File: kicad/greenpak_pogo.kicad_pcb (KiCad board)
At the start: 2 copper layers, 7.6 x 14.5 mm, 6 parts, among them J1 JST_SH_SM04B-SRSS-TB_1x04-1MP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, J2 GREENPAK_POGO_PINS

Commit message: Generated gervers.
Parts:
- turned R1 to -90 degrees
- turned R2 to -90 degrees
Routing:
- net VCC: track 7.47 -> 15.1 mm
- net /SDA: track 13.0 -> 13.6 mm
- net /SCL: track 7.75 -> 8.31 mm
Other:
- board text added: "V0.2"
- board text removed: "V0.1"
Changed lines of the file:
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@@
     (fp_line (start 3 -1.675) (end 3 2.575)
       (stroke (width 0.1) (type solid)) (layer "F.Fab"))
-    (pad "" thru_hole roundrect locked (at -2.8 1.875) (size 1.2 1.8) (drill 0.3) (layers "*.Cu" "F.Paste" "F.Mask") (roundrect_rratio 0.208333))
-    (pad "" thru_hole roundrect locked (at 2.8 1.875) (size 1.2 1.8) (drill 0.3) (layers "*.Cu" "F.Paste" "F.Mask") (roundrect_rratio 0.208333))
+    (pad "" thru_hole roundrect locked (at -2.8 1.875) (size 1.2 1.8) (drill 0.3) (layers "*.Cu" "F.Paste" "F.Mask") (roundrect_rratio 0.2083333333))
+    (pad "" thru_hole roundrect locked (at 2.8 1.875) (size 1.2 1.8) (drill 0.3) (layers "*.Cu" "F.Paste" "F.Mask") (roundrect_rratio 0.2083333333))
     (pad "1" thru_hole roundrect locked (at -1.5 -2) (size 0.6 1.55) (drill 0.3) (layers "*.Cu" "F.Paste" "F.Mask") (roundrect_rratio 0.25)
       (net 1 "GNDD") (pinfunction "Pin_1") (pintype "passive"))
@@
   )
   (footprint "greenpak_pogo:R_0402_1005Metric" (layer "F.Cu")
-    (at 2.54 3.556 90)
+    (at 2.54 3.556 -90)
     (descr "Resistor SMD 0402 (1005 Metric), square (rectangular) end terminal, IPC_7351 nominal, (Body size source: IPC-SM-782 page 72, https://www.pcb-3d.com/wordpress/wp-content/uploads/ipc-sm-782a_amendment_1_and_2.pdf), generated with kicad-footprint-generator")
     (tags "resistor")
@@
     (fp_line (start 0.525 0.27) (end -0.525 0.27)
       (stroke (width 0.1) (type solid)) (layer "F.Fab"))
-    (pad "1" smd roundrect (at -0.51 0 90) (size 0.54 0.64) (layers "F.Cu" "F.Paste" "F.Mask") (roundrect_rratio 0.25)
+    (pad "1" smd roundrect (at -0.51 0 270) (size 0.54 0.64) (layers "F.Cu" "F.Paste" "F.Mask") (roundrect_rratio 0.25)
       (net 5 "VCC") (pintype "passive"))
-    (pad "2" smd roundrect (at 0.51 0 90) (size 0.54 0.64) (layers "F.Cu" "F.Paste" "F.Mask") (roundrect_rratio 0.25)
+    (pad "2" smd roundrect (at 0.51 0 270) (size 0.54 0.64) (layers "F.Cu" "F.Paste" "F.Mask") (roundrect_rratio 0.25)
       (net 4 "/SCL") (pintype "passive"))
     (model "${KICAD6_3DMODEL_DIR}/Resistor_SMD.3dshapes/R_0402_1005Metric.wrl"
@@
   )
   (footprint "greenpak_pogo:R_0402_1005Metric" (layer "F.Cu")
-    (at -2.54 3.556 90)
+    (at -2.54 3.556 -90)
     (descr "Resistor SMD 0402 (1005 Metric), square (rectangular) end terminal, IPC_7351 nominal, (Body size source: IPC-SM-782 page 72, https://www.pcb-3d.com/wordpress/wp-content/uploads/ipc-sm-782a_amendment_1_and_2.pdf), generated with kicad-footprint-generator")
     (tags "resistor")
@@
     (fp_line (start 0.525 0.27) (end -0.525 0.27)
       (stroke (width 0.1) (type solid)) (layer "F.Fab"))
-    (pad "1" smd roundrect (at -0.51 0 90) (size 0.54 0.64) (layers "F.Cu" "F.Paste" "F.Mask") (roundrect_rratio 0.25)
+    (pad "1" smd roundrect (at -0.51 0 270) (size 0.54 0.64) (layers "F.Cu" "F.Paste" "F.Mask") (roundrect_rratio 0.25)
       (net 5 "VCC") (pintype "passive"))
-    (pad "2" smd roundrect (at 0.51 0 90) (size 0.54 0.64) (layers "F.Cu" "F.Paste" "F.Mask") (roundrect_rratio 0.25)
+    (pad "2" smd roundrect (at 0.51 0 270) (size 0.54 0.64) (layers "F.Cu" "F.Paste" "F.Mask") (roundrect_rratio 0.25)
       (net 3 "/SDA") (pintype "passive"))
     (model "${KICAD6_3DMODEL_DIR}/Resistor_SMD.3dshapes/R_0402_1005Metric.wrl"
@@
     (effects (font (size 0.75 0.75) (thickness 0.15)) (justify right mirror))
   )
-  (gr_text "V0.1" (at 0 6.858) (layer "B.SilkS")
+  (gr_text "V0.2" (at 0 6.858) (layer "B.SilkS")
     (effects (font (size 0.75 0.75) (thickness 0.15)) (justify top mirror))
   )
@@
     (effects (font (size 0.75 0.75) (thickness 0.15)) (justify right mirror))
   )
-  (gr_text locked "POGO PINS\nTHIS SIDE" (at 0 1.4732) (layer "B.SilkS")
+  (gr_text locked "POGO PINS\nTHIS SIDE" (at 0 1.397) (layer "B.SilkS")
     (effects (font (size 0.75 0.75) (thickness 0.15)) (justify top mirror))
   )
@@
     (effects (font (size 0.7 0.7) (thickness 0.1)) (justify left bottom))
   )
-  (segment (start -1.7272 1.7272) (end 0 0) (width 0.4064) (layer "F.Cu") (net 1))
-  (segment (start -1.7272 4.6228) (end -1.7272 1.7272) (width 0.4064) (layer "F.Cu") (net 1))
-  (segment (start -1.5 4.85) (end -1.7272 4.6228) (width 0.4064) (layer "F.Cu") (net 1))
-  (segment (start -1.5 5.62) (end -1.5 4.85) (width 0.4064) (layer "F.Cu") (net 1))
+  (segment (start -1.7272 2.6924) (end 0 0.9652) (width 0.4064) (layer "F.Cu") (net 1))
+  (segment (start -1.5 5.62) (end -1.5 4.7632) (width 0.4064) (layer "F.Cu") (net 1))
+  (segment (start -1.7272 4.536) (end -1.7272 2.6924) (width 0.4064) (layer "F.Cu") (net 1))
+  (segment (start 0 0.9652) (end 0 0) (width 0.4064) (layer "F.Cu") (net 1))
+  (segment (start -1.5 4.7632) (end -1.7272 4.536) (width 0.4064) (layer "F.Cu") (net 1))
   (segment (start -0.65 3.175) (end -0.5 3.325) (width 0.4064) (layer "F.Cu") (net 2))
   (segment (start -0.5 3.325) (end -0.5 5.62) (width 0.4064) (layer "F.Cu") (net 2))
-  (segment (start -3.302 6.6548) (end -2.3114 7.6454) (width 0.2032) (layer "F.Cu") (net 3))
-  (segment (start -2.54 3.046) (end -3.0206 3.046) (width 0.2032) (layer "F.Cu") (net 3))
-  (segment (start -3.0206 3.046) (end -3.302 3.3274) (width 0.2032) (layer "F.Cu") (net 3))
-  (segment (start -0.254 7.6454) (end 0.508 6.8834) (width 0.2032) (layer "F.Cu") (net 3))
-  (segment (start -2.54 1.397) (end -2.54 3.046) (width 0.2032) (layer "F.Cu") (net 3))
-  (segment (start -2.3114 7.6454) (end -0.254 7.6454) (width 0.2032) (layer "F.Cu") (net 3))
+  (segment (start -2.286 1.143) (end -3.302 2.159) (width 0.2032) (layer "F.Cu") (net 3))
+  (segment (start -2.6924 4.2184) (end -2.54 4.066) (width 0.254) (layer "F.Cu") (net 3))
   (segment (start 0.508 5.8312) (end 0.508 6.858) (width 0.2032) (layer "F.Cu") (net 3))
-  (segment (start -3.302 3.3274) (end -3.302 6.6548) (width 0.2032) (layer "F.Cu") (net 3))
-  (segment (start -2.54 3.046) (end -2.5146 3.0206) (width 0.254) (layer "F.Cu") (net 3))
-  (segment (start -2.286 1.143) (end -2.54 1.397) (width 0.2032) (layer "F.Cu") (net 3))
+  (segment (start -2.54 4.066) (end -3.3 4.066) (width 0.2032) (layer "F.Cu") (net 3))
+  (segment (start 0.2032 7.4422) (end 0.508 7.1374) (width 0.2032) (layer "F.Cu") (net 3))
+  (segment (start -3.302 2.159) (end -3.302 6.6548) (width 0.2032) (layer "F.Cu") (net 3))
+  (segment (start 0.508 7.1374) (end 0.508 6.8834) (width 0.2032) (layer "F.Cu") (net 3))
+  (segment (start -2.5146 7.4422) (end 0.2032 7.4422) (width 0.2032) (layer "F.Cu") (net 3))
   (segment (start -2.286 0) (end -2.286 1.143) (width 0.2032) (layer "F.Cu") (net 3))
-  (segment (start 3.046 3.046) (end 2.54 3.046) (width 0.2032) (layer "F.Cu") (net 4))
-  (segment (start 2.2286 5.8232) (end 3.302 4.7498) (width 0.2032) (layer "F.Cu") (net 4))
+  (segment (start -3.302 6.6548) (end -2.5146 7.4422) (width 0.2032) (layer "F.Cu") (net 3))
+  (segment (start 2.381 5.8232) (end 3.302 4.9022) (width 0.2032) (layer "F.Cu") (net 4))
+  (segment (start 3.302 4.9022) (end 3.302 4.064) (width 0.2032) (layer "F.Cu") (net 4))
+  (segment (start 3.302 4.064) (end 3.302 2.6416) (width 0.2032) (layer "F.Cu") (net 4))
+  (segment (start 2.54 4.066) (end 3.3 4.066) (width 0.2032) (layer "F.Cu") (net 4))
   (segment (start 2.3114 0.0254) (end 2.286 0) (width 0.254) (layer "F.Cu") (net 4))
-  (segment (start 1.5 5.8232) (end 2.2286 5.8232) (width 0.2032) (layer "F.Cu") (net 4))
-  (segment (start 3.302 4.7498) (end 3.302 3.302) (width 0.2032) (layer "F.Cu") (net 4))
-  (segment (start 2.286 1.778) (end 2.54 2.032) (width 0.2032) (layer "F.Cu") (net 4))
-  (segment (start 2.286 0) (end 2.286 1.778) (width 0.2032) (layer "F.Cu") (net 4))
-  (segment (start 2.54 2.032) (end 2.54 3.046) (width 0.2032) (layer "F.Cu") (net 4))
-  (segment (start 3.302 3.302) (end 3.046 3.046) (width 0.2032) (layer "F.Cu") (net 4))
-  (segment (start -2.6924 4.2184) (end -2.54 4.066) (width 0.254) (layer "F.Cu") (net 5))
+  (segment (start 1.5 5.8232) (end 2.381 5.8232) (width 0.2032) (layer "F.Cu") (net 4))
+  (segment (start 2.286 1.6256) (end 2.286 0) (width 0.2032) (layer "F.Cu") (net 4))
+  (segment (start 3.302 2.6416) (end 2.286 1.6256) (width 0.2032) (layer "F.Cu") (net 4))
+  (segment (start 3.3 4.066) (end 3.302 4.064) (width 0.2032) (layer "F.Cu") (net 4))
   (segment (start 0.65 3.175) (end 0.65 1.8011) (width 0.3048) (layer "F.Cu") (net 5))
   (segment (start 0.65 1.8011) (end 1.1938 1.2573) (width 0.3048) (layer "F.Cu") (net 5))
   (segment (start 1.1938 -1.1557) (end 0.3175 -2.032) (width 0.3048) (layer "F.Cu") (net 5))
+  (segment (start -2.54 2.455416) (end -1.2 1.115416) (width 0.254) (layer "F.Cu") (net 5))
+  (segment (start -2.54 3.046) (end -2.5146 3.0206) (width 0.254) (layer "F.Cu") (net 5))
+  (segment (start 0.47675 3.0734) (end 2.57125 3.0734) (width 0.2032) (layer "F.Cu") (net 5))
   (segment (start 0.3175 -2.032) (end -1.143 -2.032) (width 0.3048) (layer "F.Cu") (net 5))
+  (segment (start -2.54 3.046) (end -2.54 2.455416) (width 0.254) (layer "F.Cu") (net 5))
   (segment (start 1.1938 1.2573) (end 1.1938 -1.1557) (width 0.3048) (layer "F.Cu") (net 5))
+  (segment (start -1.2 1.115416) (end -1.2 -2.1) (width 0.254) (layer "F.Cu") (net 5))
   (group "" locked (id 2972b439-deb4-4103-8004-66da0f130234)
     (members

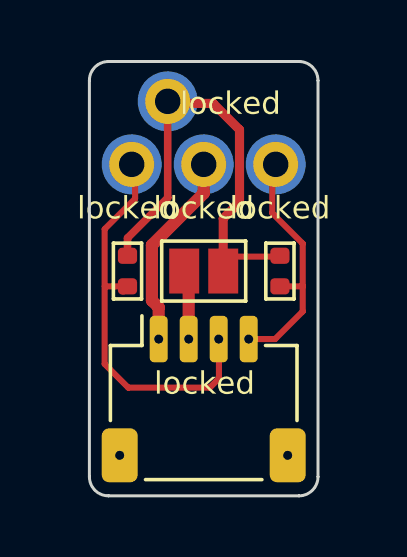
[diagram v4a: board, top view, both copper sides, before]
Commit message: Increased VCC trace width and regenerated gerbers.
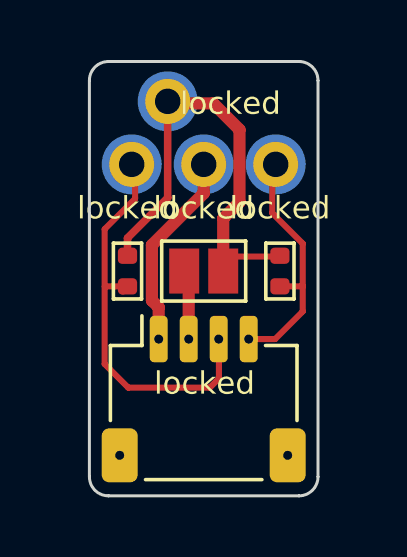
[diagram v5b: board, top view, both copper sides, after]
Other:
- board text removed: "NOTE: This PCB layout is not tied to a Kicad schematic."
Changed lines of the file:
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@@
     (effects (font (size 0.75 0.75) (thickness 0.15)) (justify top))
-  )
-  (gr_text "NOTE: This PCB layout is not tied \nto a Kicad schematic." (at -6.9088 14.9098) (layer "Cmts.User")
-    (effects (font (size 0.7 0.7) (thickness 0.1)) (justify left bottom))
   )
   (segment (start -1.7272 2.6924) (end 0 0.9652) (width 0.4064) (layer "F.Cu") (net 1))
@@
   (segment (start 3.302 2.6416) (end 2.286 1.6256) (width 0.2032) (layer "F.Cu") (net 4))
   (segment (start 3.3 4.066) (end 3.302 4.064) (width 0.2032) (layer "F.Cu") (net 4))
-  (segment (start 0.65 3.175) (end 0.65 1.8011) (width 0.3048) (layer "F.Cu") (net 5))
-  (segment (start 0.65 1.8011) (end 1.1938 1.2573) (width 0.3048) (layer "F.Cu") (net 5))
-  (segment (start 1.1938 -1.1557) (end 0.3175 -2.032) (width 0.3048) (layer "F.Cu") (net 5))
+  (segment (start 0.65 3.175) (end 0.65 1.8011) (width 0.4064) (layer "F.Cu") (net 5))
+  (segment (start 0.65 1.8011) (end 1.1938 1.2573) (width 0.4064) (layer "F.Cu") (net 5))
+  (segment (start 1.1938 -1.1557) (end 0.3175 -2.032) (width 0.4064) (layer "F.Cu") (net 5))
   (segment (start -2.54 2.455416) (end -1.2 1.115416) (width 0.254) (layer "F.Cu") (net 5))
   (segment (start -2.54 3.046) (end -2.5146 3.0206) (width 0.254) (layer "F.Cu") (net 5))
   (segment (start 0.47675 3.0734) (end 2.57125 3.0734) (width 0.2032) (layer "F.Cu") (net 5))
-  (segment (start 0.3175 -2.032) (end -1.143 -2.032) (width 0.3048) (layer "F.Cu") (net 5))
+  (segment (start 0.3175 -2.032) (end -1.143 -2.032) (width 0.4064) (layer "F.Cu") (net 5))
   (segment (start -2.54 3.046) (end -2.54 2.455416) (width 0.254) (layer "F.Cu") (net 5))
-  (segment (start 1.1938 1.2573) (end 1.1938 -1.1557) (width 0.3048) (layer "F.Cu") (net 5))
+  (segment (start 1.1938 1.2573) (end 1.1938 -1.1557) (width 0.4064) (layer "F.Cu") (net 5))
   (segment (start -1.2 1.115416) (end -1.2 -2.1) (width 0.254) (layer "F.Cu") (net 5))
   (group "" locked (id 2972b439-deb4-4103-8004-66da0f130234)
